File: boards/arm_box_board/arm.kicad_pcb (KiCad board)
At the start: 2 copper layers, 5 parts, among them J1 Output, J2 24V, U1 Teensy4.1, U2 PololuD24V5F5, U3 TMC2209_SILENTSTEPSTICK

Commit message: Updated Arm board with ethernet
updated on 04/24
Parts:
- added C1: C_Small, Capacitor_THT:C_Rect_L4.0mm_W2.5mm_P2.50mm, F.Cu at (116.5, 100.8)
- added J3: J00-0045NL, EthernetConn:PULSE_J00-0045NL, F.Cu at (127.4, 101.4)
- moved U2 15.6 mm to (108.4, 96.5), turned to 90 degrees
- moved J1 12.5 mm to (108.4, 92.5), turned to 90 degrees
- moved J2 4.00 mm to (98.7, 94.1)
- moved U3 0.80 mm to (84.9, 100.8)
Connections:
- U1 pad 60: unconnected-(U1-R+-Pad60) -> Net-(J3-CTT)
- U1 pad 61: unconnected-(U1-LED-Pad61) -> Net-(J3-LC)
- U1 pad 62: unconnected-(U1-T--Pad62) -> Net-(J3-RD+)
- U1 pad 63: unconnected-(U1-T+-Pad63) -> Net-(J3-TD+)
- U1 pad 64: unconnected-(U1-GND-Pad64) -> Net-(J3-GND)
- U1 pad 65: unconnected-(U1-R--Pad65) -> Net-(J3-RD-)
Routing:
- net Net-(J3-GND): track 0.00 -> 74.3 mm
- net Net-(J3-LC): track 0.00 -> 71.3 mm
- net Net-(J3-RD-): track 0.00 -> 47.1 mm
- net Net-(J3-CTT): track 0.00 -> 46.5 mm
- net Net-(J3-RD+): track 0.00 -> 44.6 mm
- net Net-(J3-TD+): track 0.00 -> 39.3 mm
- net Net-(J3-CTR): track 0.00 -> 16.9 mm
- net Net-(J2-Pin_2): track 37.9 -> 26.6 mm
- net Net-(J1-Pin_4): track 38.0 -> 48.9 mm
- net Net-(J2-Pin_1): track 109.4 -> 99.7 mm
- net Net-(J1-Pin_3): track 34.6 -> 43.2 mm
- net Net-(J1-Pin_2): track 30.8 -> 34.2 mm
- net Net-(U1-VIN): track 67.1 -> 65.5 mm
- net Net-(J1-Pin_1): track 27.2 -> 25.8 mm
- net Net-(U1-1_TX1_CTX2_MISO1): track 14.3 -> 13.5 mm
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
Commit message: update
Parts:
- C1: footprint Capacitor_THT:C_Rect_L4.0mm_W2.5mm_P2.50mm -> Capacitor_THT:C_Disc_D3.0mm_W1.6mm_P2.50mm
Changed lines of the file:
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@@
 	)
 	(setup
+		(stackup
+			(layer "F.SilkS"
+				(type "Top Silk Screen")
+			)
+			(layer "F.Paste"
+				(type "Top Solder Paste")
+			)
+			(layer "F.Mask"
+				(type "Top Solder Mask")
+				(thickness 0.01)
+			)
+			(layer "F.Cu"
+				(type "copper")
+				(thickness 0.035)
+			)
+			(layer "dielectric 1"
+				(type "core")
+				(thickness 1.51)
+				(material "FR4")
+				(epsilon_r 4.5)
+				(loss_tangent 0.02)
+			)
+			(layer "B.Cu"
+				(type "copper")
+				(thickness 0.035)
+			)
+			(layer "B.Mask"
+				(type "Bottom Solder Mask")
+				(thickness 0.01)
+			)
+			(layer "B.Paste"
+				(type "Bottom Solder Paste")
+			)
+			(layer "B.SilkS"
+				(type "Bottom Silk Screen")
+			)
+			(copper_finish "None")
+			(dielectric_constraints no)
+		)
 		(pad_to_mask_clearance 0)
 		(allow_soldermask_bridges_in_footprints no)
@@
 		)
 	)
-	(footprint "Capacitor_THT:C_Rect_L4.0mm_W2.5mm_P2.50mm"
+	(footprint "Capacitor_THT:C_Disc_D3.0mm_W1.6mm_P2.50mm"
 		(layer "F.Cu")
 		(at 116.5 100.75 -90)
-		(descr "C, Rect series, Radial, pin pitch=2.50mm, , length*width=4*2.5mm^2, Capacitor")
-		(tags "C Rect series Radial pin pitch 2.50mm  length 4mm width 2.5mm Capacitor")
+		(descr "C, Disc series, Radial, pin pitch=2.50mm, , diameter*width=3.0*1.6mm^2, Capacitor, http://www.vishay.com/docs/45233/krseries.pdf")
+		(tags "C Disc series Radial pin pitch 2.50mm  diameter 3.0mm width 1.6mm Capacitor")
 		(property "Reference" "C1"
-			(at 1.25 -2.5 90)
+			(at 1.25 -2.05 -90)
 			(layer "F.SilkS")
 			(effects
@@
 		)
 		(property "Value" "C_Small"
-			(at 2.75 2.5 90)
+			(at 1.25 2.05 -90)
 			(layer "F.Fab")
 			(effects
@@
 			)
 		)
-		(property "Footprint" "Capacitor_THT:C_Rect_L4.0mm_W2.5mm_P2.50mm"
+		(property "Footprint" "Capacitor_THT:C_Disc_D3.0mm_W1.6mm_P2.50mm"
 			(at 0 0 -90)
 			(unlocked yes)
@@
 		(attr through_hole)
 		(fp_line
-			(start -0.87 1.37)
-			(end 3.37 1.37)
-			(stroke
-				(width 0.12)
-				(type solid)
-			)
-			(layer "F.SilkS")
-		)
-		(fp_line
-			(start -0.87 0.665)
-			(end -0.87 1.37)
-			(stroke
-				(width 0.12)
-				(type solid)
-			)
-			(layer "F.SilkS")
-		)
-		(fp_line
-			(start 3.37 0.665)
-			(end 3.37 1.37)
+			(start 0.621 0.92)
+			(end 1.879 0.92)
 			(stroke
 				(width 0.12)
@@
 		)
 		(fp_line
-			(start -0.87 -1.37)
-			(end -0.87 -0.665)
+			(start 0.621 -0.92)
+			(end 1.879 -0.92)
 			(stroke
 				(width 0.12)
@@
 		)
 		(fp_line
-			(start -0.87 -1.37)
-			(end 3.37 -1.37)
-			(stroke
-				(width 0.12)
-				(type solid)
-			)
-			(layer "F.SilkS")
-		)
-		(fp_line
-			(start 3.37 -1.37)
-			(end 3.37 -0.665)
-			(stroke
-				(width 0.12)
-				(type solid)
-			)
-			(layer "F.SilkS")
-		)
-		(fp_line
-			(start -1.05 1.5)
-			(end 3.55 1.5)
+			(start -1.05 1.05)
+			(end 3.55 1.05)
 			(stroke
 				(width 0.05)
@@
 		)
 		(fp_line
-			(start 3.55 1.5)
-			(end 3.55 -1.5)
+			(start 3.55 1.05)
+			(end 3.55 -1.05)
 			(stroke
 				(width 0.05)
@@
 		)
 		(fp_line
-			(start -1.05 -1.5)
-			(end -1.05 1.5)
+			(start -1.05 -1.05)
+			(end -1.05 1.05)
 			(stroke
 				(width 0.05)
@@
 		)
 		(fp_line
-			(start 3.55 -1.5)
-			(end -1.05 -1.5)
+			(start 3.55 -1.05)
+			(end -1.05 -1.05)
 			(stroke
 				(width 0.05)
@@
 		)
 		(fp_line
-			(start -0.75 1.25)
-			(end 3.25 1.25)
+			(start -0.25 0.8)
+			(end 2.75 0.8)
 			(stroke
 				(width 0.1)
@@
 		)
 		(fp_line
-			(start 3.25 1.25)
-			(end 3.25 -1.25)
+			(start 2.75 0.8)
+			(end 2.75 -0.8)
 			(stroke
 				(width 0.1)
@@
 		)
 		(fp_line
-			(start -0.75 -1.25)
-			(end -0.75 1.25)
+			(start -0.25 -0.8)
+			(end -0.25 0.8)
 			(stroke
 				(width 0.1)
@@
 		)
 		(fp_line
-			(start 3.25 -1.25)
-			(end -0.75 -1.25)
+			(start 2.75 -0.8)
+			(end -0.25 -0.8)
 			(stroke
 				(width 0.1)
@@
 		)
 		(fp_text user "${REFERENCE}"
-			(at 1.25 0 90)
+			(at 1.25 0 -90)
 			(layer "F.Fab")
 			(effects
 				(font
-					(size 0.8 0.8)
-					(thickness 0.12)
+					(size 0.6 0.6)
+					(thickness 0.09)
 				)
 			)
@@
 			(pintype "passive")
 		)
-		(model "${KICAD8_3DMODEL_DIR}/Capacitor_THT.3dshapes/C_Rect_L4.0mm_W2.5mm_P2.50mm.wrl"
+		(model "${KICAD8_3DMODEL_DIR}/Capacitor_THT.3dshapes/C_Disc_D3.0mm_W1.6mm_P2.50mm.wrl"
 			(offset
 				(xyz 0 0 0)
@@
 		)
 	)
+	(gr_rect
+		(start 69.5 67)
+		(end 139.5 117)
+		(stroke
+			(width 0.2)
+			(type default)
+		)
+		(fill none)
+		(layer "B.Cu")
+	)
 	(segment

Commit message: cap added
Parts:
- added C2: C_Large, Capacitor_THT:CP_Radial_D4.0mm_P1.50mm, F.Cu at (108.5, 101.5)
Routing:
- net Net-(J2-Pin_1): track 99.7 -> 106.2 mm
- net Net-(J2-Pin_2): track 26.6 -> 32.6 mm

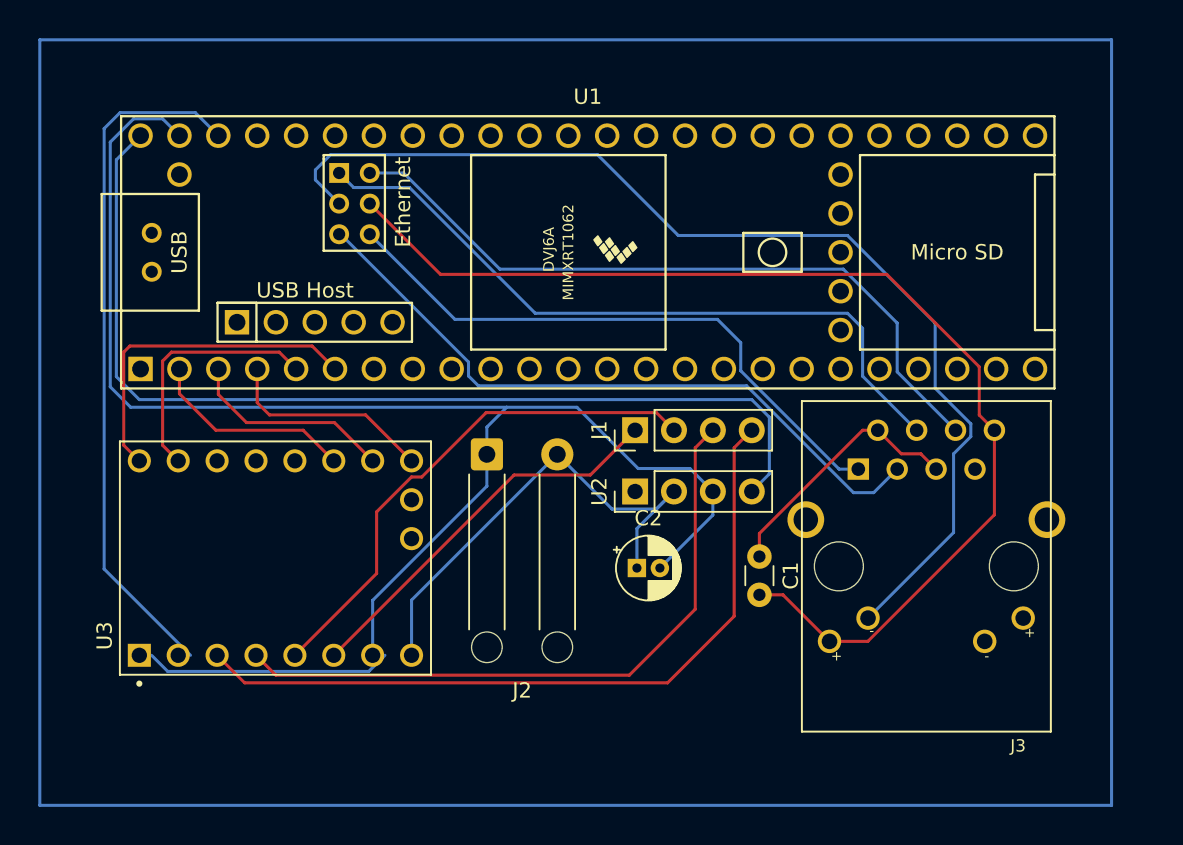
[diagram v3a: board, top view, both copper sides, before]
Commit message: Corrected Ethernet pin matches to teensy
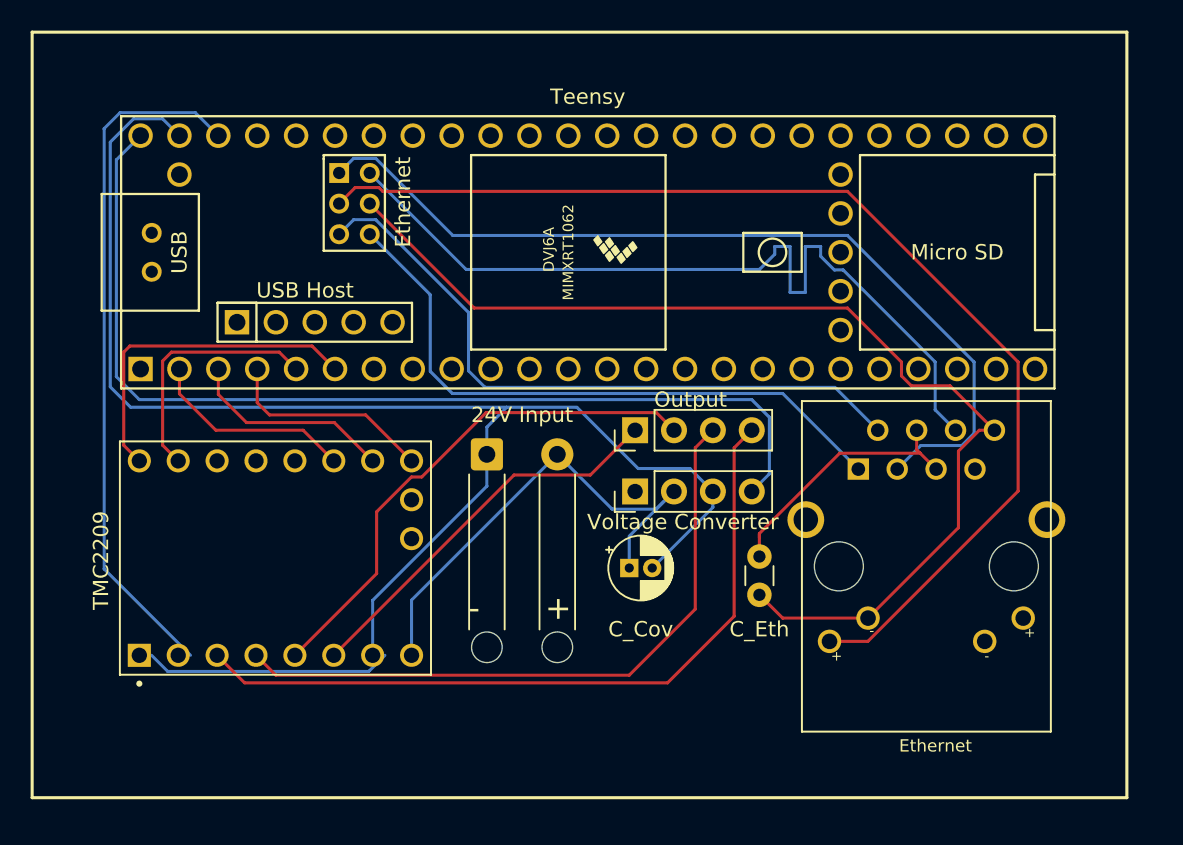
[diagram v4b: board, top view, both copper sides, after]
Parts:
- removed C2: C_Large, Capacitor_THT:CP_Radial_D4.0mm_P1.50mm
- added C_Cov: C_Large, Capacitor_THT:CP_Radial_D4.0mm_P1.50mm, F.Cu at (108.0, 101.5)
- 24V Input: renamed from J2
- Voltage Converter: renamed from U2
- renumbered C1 to C_Eth, J3 to Ethernet, J1 to Output, U3 to TMC2209, U1 to Teensy
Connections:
- Ethernet pad 10: Net-(J3-LC) -> Net-(J3-GND)
- Ethernet pad 2: Net-(J3-CTR) -> Net-(J3-TD-)
- Ethernet pad 4: Net-(J3-CTT) -> Net-(J3-CTR)
- Ethernet pad 9: Net-(J3-GND) -> Net-(J3-LA)
- Teensy pad 60: Net-(J3-CTT) -> Net-(J3-RD+)
- Teensy pad 61: Net-(J3-LC) -> Net-(J3-LA)
- Teensy pad 62: Net-(J3-RD+) -> Net-(J3-TD-)
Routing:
- net Net-(J3-LA): track 0.00 -> 74.3 mm
- net Net-(J3-LC): track 71.3 -> 0.00 mm
- net Net-(J3-CTT): track 46.5 -> 0.00 mm
- net Net-(J3-TD-): track 0.00 -> 43.6 mm
- net Net-(J3-RD+): track 44.6 -> 58.0 mm
- net Net-(J3-RD-): track 47.1 -> 55.0 mm
- net Net-(J3-GND): track 74.3 -> 72.0 mm
- net Net-(J3-TD+): track 39.3 -> 41.2 mm
- net Net-(J3-CTR): track 16.9 -> 17.5 mm
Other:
- board text added: "+"
- board text added: "-"

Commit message: Extra pins/labels added
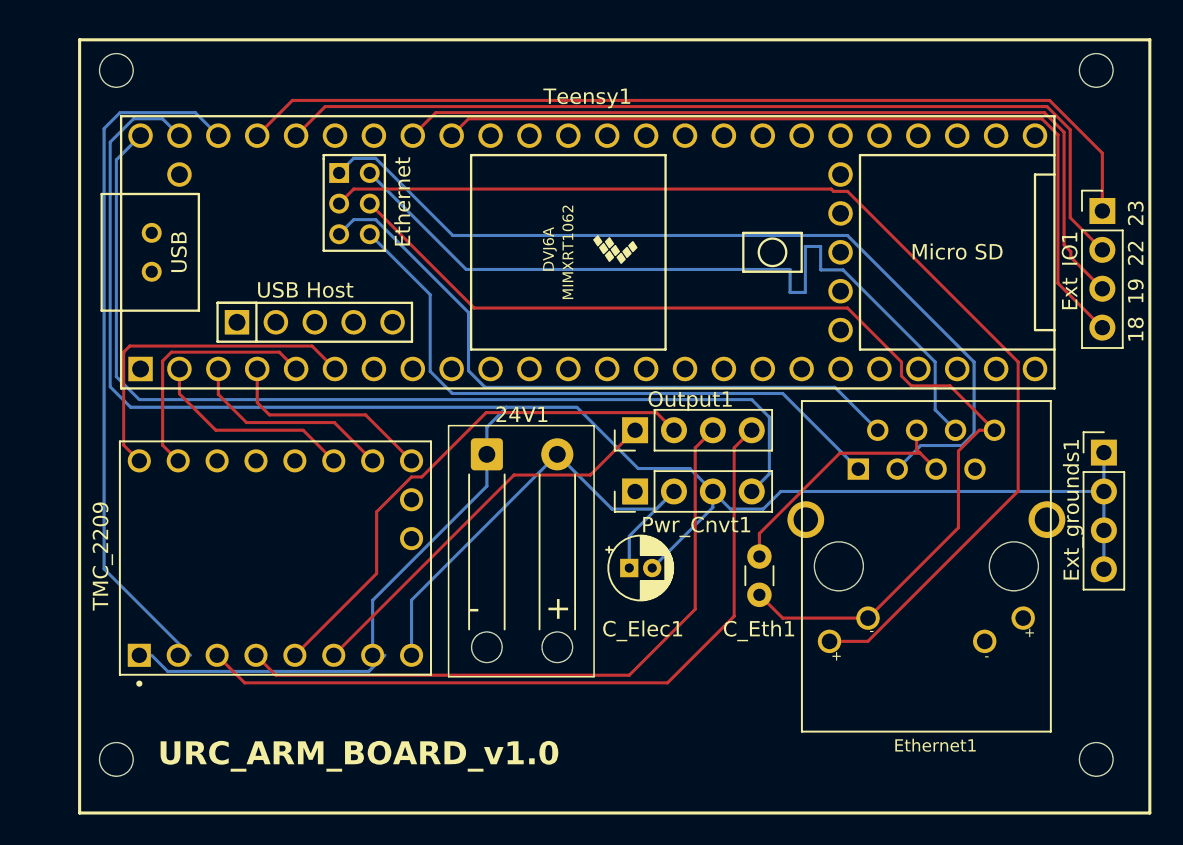
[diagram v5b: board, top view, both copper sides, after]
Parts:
- added ?: , , F.Cu at (138.5, 69.0)
- added ?: , , F.Cu at (74.5, 114.0)
- added ?: , , F.Cu at (138.5, 114.0)
- added ?: , , F.Cu at (74.5, 69.0)
- added Ext_IO1: Output, Connector_PinHeader_2.54mm:PinHeader_1x04_P2.54mm_Vertical, F.Cu at (138.9, 78.2)
- added Ext_grounds1: Output, Connector_PinHeader_2.54mm:PinHeader_1x04_P2.54mm_Vertical, F.Cu at (139.0, 94.0)
- 24V1: renamed from 24V Input
- Pwr_Cnvt1: renamed from Voltage Converter
- renumbered C_Cov to C_Elec1, C_Eth to C_Eth1, Ethernet to Ethernet1, Output to Output1, TMC2209 to TMC_2209, Teensy to Teensy1
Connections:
- Teensy1 pad 40: unconnected-(U1-18_A4_SDA-Pad40) -> Net-(Ext_IO1-Pin_4)
- Teensy1 pad 41: unconnected-(U1-19_A5_SCL-Pad41) -> Net-(Ext_IO1-Pin_3)
- Teensy1 pad 44: unconnected-(U1-22_A8_CTX1-Pad44) -> Net-(Ext_IO1-Pin_2)
- Teensy1 pad 45: unconnected-(U1-23_A9_CRX1_MCLK1-Pad45) -> Net-(Ext_IO1-Pin_1)
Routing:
- net Net-(Ext_IO1-Pin_1): track 0.00 -> 61.4 mm
- net Net-(Ext_IO1-Pin_2): track 0.00 -> 60.7 mm
- net Net-(Ext_IO1-Pin_3): track 0.00 -> 54.9 mm
- net Net-(Ext_IO1-Pin_4): track 0.00 -> 54.3 mm
- net Net-(24V1-Pin_1): track 106.4 -> 140.5 mm
- net Net-(Ethernet1-RD-): track 55.0 -> 53.1 mm
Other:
- board text added: "18"
- board text added: "19"
- board text added: "22"
- board text added: "23"
- board text added: "URC_ARM_BOARD_v1.0"
